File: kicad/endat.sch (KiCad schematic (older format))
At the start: 29 parts, among them J1901 tblock2x6, U1901 SI8662BD, U1904 SN75C1168DBR, U1905 SN75C1168DBR, U1908 SI8662BD

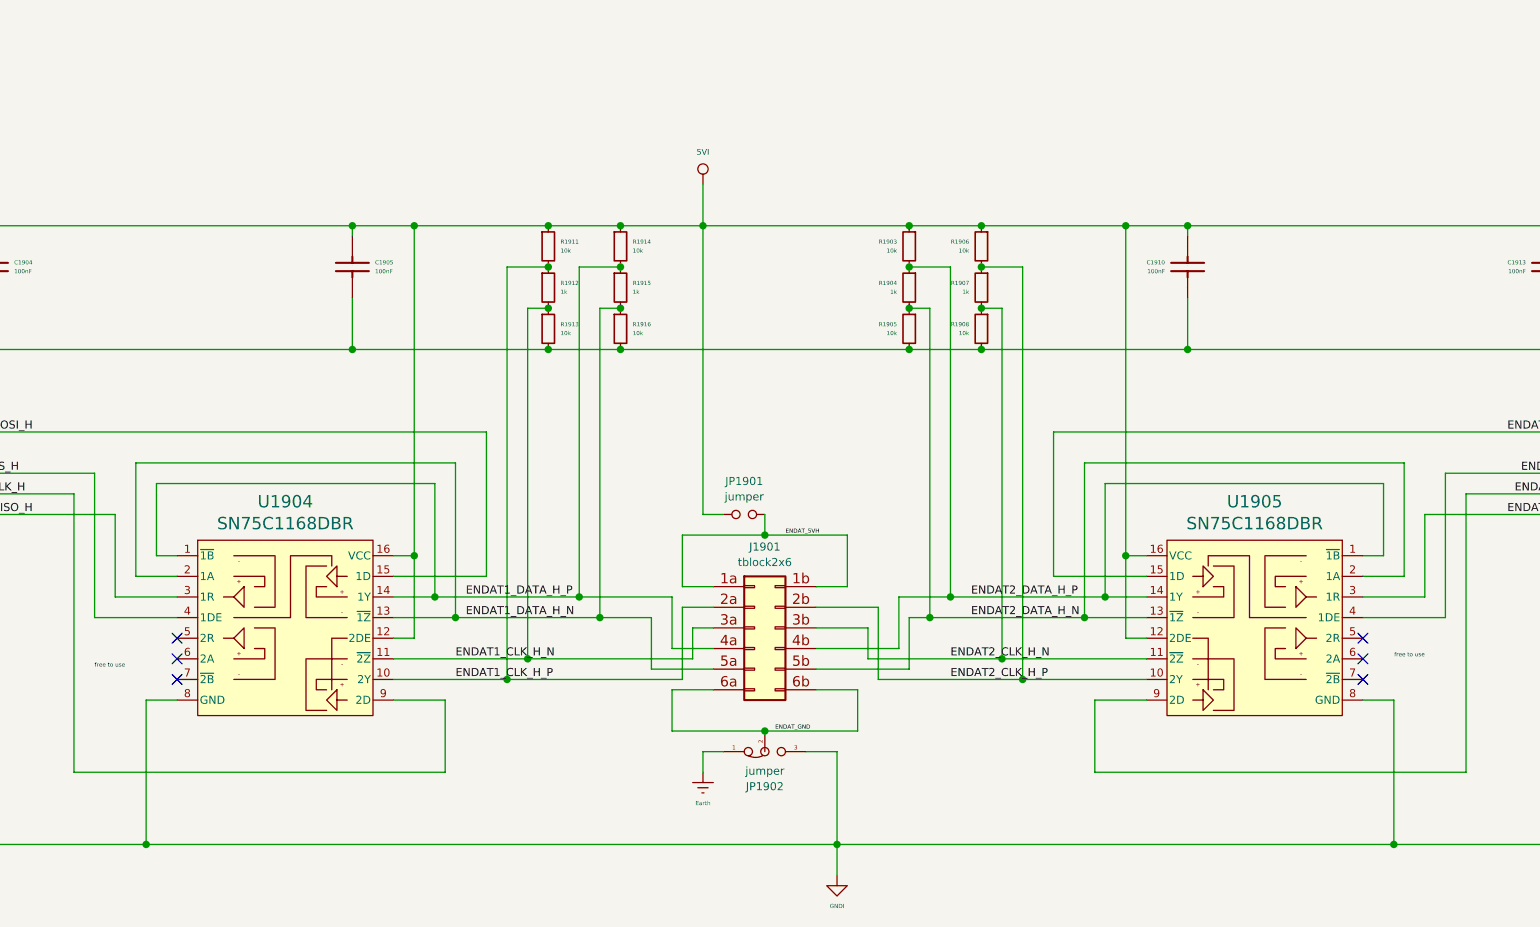
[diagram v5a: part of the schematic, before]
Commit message: added sloted holes everyware
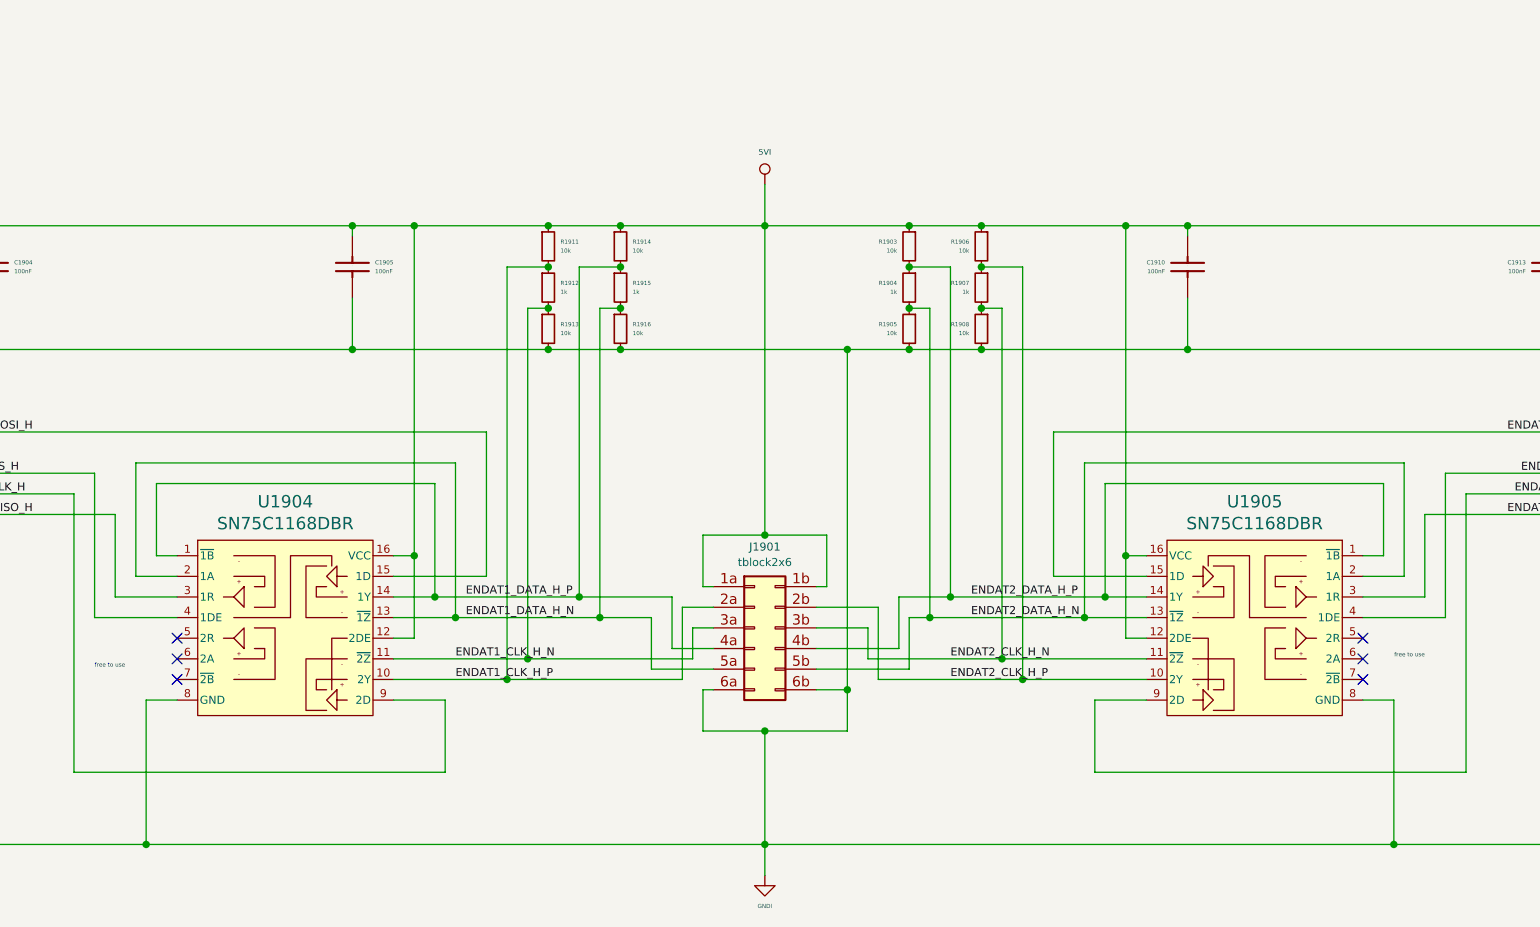
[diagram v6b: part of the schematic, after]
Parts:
- removed JP1901: jumper, servo:SolderJumper-2_P1.3mm_Open_RoundedPad1.0x1.5mm, symbol servo:jumper
- removed JP1902: jumper, Jumper:SolderJumper-3_P1.3mm_Open_RoundedPad1.0x1.5mm, symbol servo:Jumper_3_Bridged12
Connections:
- net ENDAT_5VH is gone; now on net 5VI: J1901.1a (Pin_1a), J1901.1b (Pin_1b)
- net ENDAT_GND is gone; now on net GNDI: J1901.6a (Pin_6a), J1901.6b (Pin_6b)
- net GNDI: now also C1904.1, C1905.1, C1910.1, C1913.1, R1905.2, R1908.2, R1913.2, R1916.2
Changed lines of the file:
@@
 free to use\n
 Wire Wire Line
-	8050 4550 8150 4550
-Wire Wire Line
-	7900 5400 8100 5400
+	8050 5400 8100 5400
 $Comp
 L servo:tblock2x6 J?
@@
 ENDAT1_CS_H
 Wire Wire Line
-	8100 4900 7950 4900
-Wire Wire Line
-	7950 4900 7950 4650
-Wire Wire Line
-	8750 4650 8750 4900
-Wire Wire Line
-	8750 4900 8600 4900
+	8100 4900 8050 4900
+Wire Wire Line
+	8050 4900 8050 4650
+Wire Wire Line
+	8650 4650 8650 4900
+Wire Wire Line
+	8650 4900 8600 4900
 Wire Wire Line
 	4300 4150 7000 4150
@@
 	9250 3350 9050 3350
 Connection ~ 9050 3350
-$Comp
-L servo:Jumper_3_Bridged12 JP?
-U 1 1 5E31EACF
-P 8350 5700
-AR Path="/5E1BAEAA/5E31EACF" Ref="JP?"  Part="1"
-AR Path="/5E21534F/5E31EACF" Ref="JP?"  Part="1"
-AR Path="/5DE3DF56/5E31EACF" Ref="JP?"  Part="1"
-AR Path="/5F8D42C2/5E31EACF" Ref="JP1902"  Part="1"
-F 0 "JP1902" H 8350 5869 39  0000 C CNN
-F 1 "jumper" H 8350 5794 39  0000 C CNN
-F 2 "Jumper:SolderJumper-3_P1.3mm_Open_RoundedPad1.0x1.5mm" H 8150 5500 50  0001 C CNN
-F 3 "~" H 8250 5600 50  0001 C CNN
-	1    8350 5700
-	1    0    0    1
-$EndComp
-Wire Wire Line
-	8550 5700 8700 5700
-$Comp
-L servo:Earth #PWR?
-U 1 1 5E31EAD8
-P 8050 5800
-AR Path="/5E21534F/5E31EAD8" Ref="#PWR?"  Part="1"
-AR Path="/5DE3DF56/5E31EAD8" Ref="#PWR?"  Part="1"
-AR Path="/5F8D42C2/5E31EAD8" Ref="#PWR0269"  Part="1"
-F 0 "#PWR0269" H 8050 5550 20  0001 C CNN
-F 1 "Earth" H 8050 5650 20  0000 C CNN
-F 2 "" H 8050 5800 50  0001 C CNN
-F 3 "~" H 8050 5800 50  0001 C CNN
-	1    8050 5800
-	1    0    0    -1
-$EndComp
-Wire Wire Line
-	7900 5600 8350 5600
-Wire Wire Line
-	7900 5400 7900 5600
-Wire Wire Line
-	8800 5400 8800 5600
-Connection ~ 8350 5600
-Wire Wire Line
-	8350 5600 8800 5600
+Wire Wire Line
+	8050 5400 8050 5600
+Wire Wire Line
+	8750 5400 8750 5600
 Text Label 6900 4950 0    39   ~ 0
 ENDAT1_DATA_H_P
@@
 ENDAT2_CLK_H_P
 Wire Wire Line
-	8600 5400 8800 5400
-$Comp
-L servo:jumper JP?
-U 1 1 5E2E6204
-P 8250 4550
-AR Path="/5DD76B18/5E2E6204" Ref="JP?"  Part="1"
-AR Path="/5F8D42C2/5E2E6204" Ref="JP1901"  Part="1"
-F 0 "JP1901" H 8250 4711 39  0000 C CNN
-F 1 "jumper" H 8250 4636 39  0000 C CNN
-F 2 "servo:SolderJumper-2_P1.3mm_Open_RoundedPad1.0x1.5mm" H 8150 4530 50  0001 C CNN
-F 3 "~" H 8250 4630 50  0001 C CNN
-	1    8250 4550
-	1    0    0    -1
-$EndComp
-Wire Wire Line
-	7950 4650 8350 4650
-Wire Wire Line
-	8350 4550 8350 4650
-Connection ~ 8350 4650
-Wire Wire Line
-	8350 4650 8750 4650
-Wire Wire Line
-	8050 5800 8050 5700
-Wire Wire Line
-	8050 5700 8150 5700
-Text Label 8450 4650 0    20   ~ 0
-ENDAT_5VH
-Text Label 8400 5600 0    20   ~ 0
-ENDAT_GND
+	8600 5400 8750 5400
 Text Label 4350 4150 0    39   ~ 0
 ENDAT1_MOSI_H
@@
 L servo:5VI #PWR?
 U 1 1 5E5DC4DB
-P 8050 2950
-F 0 "#PWR?" H 8050 2750 20  0001 C CNN
-F 1 "5VI" H 8050 3107 28  0000 C CNN
-F 2 "" H 8050 2950 50  0001 C CNN
-F 3 "" H 8050 2950 50  0001 C CNN
-	1    8050 2950
-	1    0    0    -1
-$EndComp
-Wire Wire Line
-	8050 2950 8050 3150
+P 8350 2950
+AR Path="/5DD76B18/5E5DC4DB" Ref="#PWR?"  Part="1"
+AR Path="/5F8D42C2/5E5DC4DB" Ref="#PWR0148"  Part="1"
+F 0 "#PWR0148" H 8350 2750 20  0001 C CNN
+F 1 "5VI" H 8350 3107 28  0000 C CNN
+F 2 "" H 8350 2950 50  0001 C CNN
+F 3 "" H 8350 2950 50  0001 C CNN
+	1    8350 2950
+	1    0    0    -1
+$EndComp
+Wire Wire Line
+	8350 2950 8350 3150
 Wire Wire Line
 	9400 3150 9050 3150
@@
 Connection ~ 9050 3150
 Wire Wire Line
-	9050 3150 8050 3150
-Connection ~ 8050 3150
-Wire Wire Line
-	8050 3150 8050 4550
-Wire Wire Line
-	8050 3150 7650 3150
+	9050 3150 8350 3150
 Wire Wire Line
 	7300 3150 6650 3150
@@
 Wire Wire Line
 	9400 3750 9050 3750
-Wire Wire Line
-	9050 3750 7650 3750
 Connection ~ 9050 3750
 Connection ~ 7650 3750
 $Comp
-L servo:GNDI #PWR?
+L servo:GNDI #PWR0149
 U 1 1 5E670415
-P 8700 6300
-F 0 "#PWR?" H 8700 6050 30  0001 C CNN
-F 1 "GNDI" H 8700 6151 20  0000 C CNN
-F 2 "" H 8700 6300 50  0001 C CNN
-F 3 "" H 8700 6300 50  0001 C CNN
-	1    8700 6300
-	1    0    0    -1
-$EndComp
-Wire Wire Line
-	8700 5700 8700 6150
-Wire Wire Line
-	11400 6150 8700 6150
+P 8350 6300
+F 0 "#PWR0149" H 8350 6050 30  0001 C CNN
+F 1 "GNDI" H 8350 6151 20  0000 C CNN
+F 2 "" H 8350 6300 50  0001 C CNN
+F 3 "" H 8350 6300 50  0001 C CNN
+	1    8350 6300
+	1    0    0    -1
+$EndComp
 Wire Wire Line
 	11400 5450 11400 6150
-Connection ~ 8700 6150
-Wire Wire Line
-	8700 6150 8700 6300
-Wire Wire Line
-	5350 6150 8700 6150
+Wire Wire Line
+	8350 6150 8350 6300
+Wire Wire Line
+	5350 6150 8350 6150
 Wire Wire Line
 	5350 5450 5350 6150
@@
 Connection ~ 4600 3150
 Connection ~ 6350 3150
+Wire Wire Line
+	8050 4650 8350 4650
+Connection ~ 8350 4650
+Wire Wire Line
+	8350 4650 8650 4650
+Wire Wire Line
+	8350 3150 8350 4650
+Connection ~ 8350 3150
+Wire Wire Line
+	7650 3150 8350 3150
+Wire Wire Line
+	8050 5600 8350 5600
+Connection ~ 8350 6150
+Wire Wire Line
+	8350 6150 11400 6150
+Wire Wire Line
+	8350 5600 8350 6150
+Connection ~ 8350 5600
+Wire Wire Line
+	8350 5600 8750 5600
+Wire Wire Line
+	8750 5400 8750 3750
+Wire Wire Line
+	7650 3750 8750 3750
+Connection ~ 8750 5400
+Connection ~ 8750 3750
+Wire Wire Line
+	8750 3750 9050 3750
 $EndSCHEMATC

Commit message: serigrafia...
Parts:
- R1901, R1902, R1903, R1904, R1905, R1906, R1907, R1908, R1911, R1912, R1913, R1914, R1915, R1916, R1931, R1932: footprint Resistor_SMD:R_0603_1608Metric -> servo:R_0603_1608Metric
- U1904, U1905: footprint Package_SO:SOIC-16W_5.3x10.2mm_P1.27mm -> servo:SOIC-16W_5.3x10.2mm_P1.27mm
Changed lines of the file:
@@
 F 0 "U1904" H 6025 5712 60  0000 C CNN
 F 1 "SN75C1168DBR" H 6025 5606 60  0000 C CNN
-F 2 "Package_SO:SOIC-16W_5.3x10.2mm_P1.27mm" H 5900 5665 60  0001 C CNN
+F 2 "servo:SOIC-16W_5.3x10.2mm_P1.27mm" H 5900 5665 60  0001 C CNN
 F 3 "../doc/datasheets/sn65c1168.pdf" H 5900 5825 60  0001 C CNN
 	1    6000 5100
@@
 F 0 "R1902" H 2900 5815 20  0000 C CNN
 F 1 "0e(dnp)" H 2900 5772 20  0000 C CNN
-F 2 "Resistor_SMD:R_0603_1608Metric" H 2400 5600 60  0001 C CNN
+F 2 "servo:R_0603_1608Metric" H 2400 5600 60  0001 C CNN
 F 3 "" H 2500 5700 60  0001 C CNN
 	1    2900 5700
@@
 F 0 "R1901" H 2500 5815 20  0000 C CNN
 F 1 "0e" H 2500 5772 20  0000 C CNN
-F 2 "Resistor_SMD:R_0603_1608Metric" H 2000 5600 60  0001 C CNN
+F 2 "servo:R_0603_1608Metric" H 2000 5600 60  0001 C CNN
 F 3 "" H 2100 5700 60  0001 C CNN
 	1    2500 5700
@@
 F 0 "U1905" H 10775 5712 60  0000 C CNN
 F 1 "SN75C1168DBR" H 10775 5606 60  0000 C CNN
-F 2 "Package_SO:SOIC-16W_5.3x10.2mm_P1.27mm" H 10650 5665 60  0001 C CNN
+F 2 "servo:SOIC-16W_5.3x10.2mm_P1.27mm" H 10650 5665 60  0001 C CNN
 F 3 "../doc/datasheets/sn65c1168.pdf" H 10650 5825 60  0001 C CNN
 	1    10750 5100
@@
 F 0 "R1931" H 13850 5815 20  0000 C CNN
 F 1 "0e(dnp)" H 13850 5772 20  0000 C CNN
-F 2 "Resistor_SMD:R_0603_1608Metric" H 13350 5600 60  0001 C CNN
+F 2 "servo:R_0603_1608Metric" H 13350 5600 60  0001 C CNN
 F 3 "" H 13450 5700 60  0001 C CNN
 	1    13850 5700
@@
 F 0 "R1932" H 14250 5815 20  0000 C CNN
 F 1 "0e" H 14250 5772 20  0000 C CNN
-F 2 "Resistor_SMD:R_0603_1608Metric" H 13750 5600 60  0001 C CNN
+F 2 "servo:R_0603_1608Metric" H 13750 5600 60  0001 C CNN
 F 3 "" H 13850 5700 60  0001 C CNN
 	1    14250 5700
@@
 F 0 "R1911" H 7359 3272 20  0000 L CNN
 F 1 "10k" H 7359 3229 20  0000 L CNN
-F 2 "Resistor_SMD:R_0603_1608Metric" H 7300 3250 50  0001 C CNN
+F 2 "servo:R_0603_1608Metric" H 7300 3250 50  0001 C CNN
 F 3 "~" H 7300 3250 50  0001 C CNN
 	1    7300 3250
@@
 F 0 "R1912" H 7359 3472 20  0000 L CNN
 F 1 "1k" H 7359 3429 20  0000 L CNN
-F 2 "Resistor_SMD:R_0603_1608Metric" H 7300 3450 50  0001 C CNN
+F 2 "servo:R_0603_1608Metric" H 7300 3450 50  0001 C CNN
 F 3 "~" H 7300 3450 50  0001 C CNN
 	1    7300 3450
@@
 F 0 "R1913" H 7359 3672 20  0000 L CNN
 F 1 "10k" H 7359 3629 20  0000 L CNN
-F 2 "Resistor_SMD:R_0603_1608Metric" H 7300 3650 50  0001 C CNN
+F 2 "servo:R_0603_1608Metric" H 7300 3650 50  0001 C CNN
 F 3 "~" H 7300 3650 50  0001 C CNN
 	1    7300 3650
@@
 F 0 "R1914" H 7709 3272 20  0000 L CNN
 F 1 "10k" H 7709 3229 20  0000 L CNN
-F 2 "Resistor_SMD:R_0603_1608Metric" H 7650 3250 50  0001 C CNN
+F 2 "servo:R_0603_1608Metric" H 7650 3250 50  0001 C CNN
 F 3 "~" H 7650 3250 50  0001 C CNN
 	1    7650 3250
@@
 F 0 "R1915" H 7709 3472 20  0000 L CNN
 F 1 "1k" H 7709 3429 20  0000 L CNN
-F 2 "Resistor_SMD:R_0603_1608Metric" H 7650 3450 50  0001 C CNN
+F 2 "servo:R_0603_1608Metric" H 7650 3450 50  0001 C CNN
 F 3 "~" H 7650 3450 50  0001 C CNN
 	1    7650 3450
@@
 F 0 "R1916" H 7709 3672 20  0000 L CNN
 F 1 "10k" H 7709 3629 20  0000 L CNN
-F 2 "Resistor_SMD:R_0603_1608Metric" H 7650 3650 50  0001 C CNN
+F 2 "servo:R_0603_1608Metric" H 7650 3650 50  0001 C CNN
 F 3 "~" H 7650 3650 50  0001 C CNN
 	1    7650 3650
@@
 F 0 "R1906" H 9459 3272 20  0000 L CNN
 F 1 "10k" H 9459 3229 20  0000 L CNN
-F 2 "Resistor_SMD:R_0603_1608Metric" H 9400 3250 50  0001 C CNN
+F 2 "servo:R_0603_1608Metric" H 9400 3250 50  0001 C CNN
 F 3 "~" H 9400 3250 50  0001 C CNN
 	1    9400 3250
@@
 F 0 "R1907" H 9459 3472 20  0000 L CNN
 F 1 "1k" H 9459 3429 20  0000 L CNN
-F 2 "Resistor_SMD:R_0603_1608Metric" H 9400 3450 50  0001 C CNN
+F 2 "servo:R_0603_1608Metric" H 9400 3450 50  0001 C CNN
 F 3 "~" H 9400 3450 50  0001 C CNN
 	1    9400 3450
@@
 F 0 "R1908" H 9459 3672 20  0000 L CNN
 F 1 "10k" H 9459 3629 20  0000 L CNN
-F 2 "Resistor_SMD:R_0603_1608Metric" H 9400 3650 50  0001 C CNN
+F 2 "servo:R_0603_1608Metric" H 9400 3650 50  0001 C CNN
 F 3 "~" H 9400 3650 50  0001 C CNN
 	1    9400 3650
@@
 F 0 "R1903" H 9109 3272 20  0000 L CNN
 F 1 "10k" H 9109 3229 20  0000 L CNN
-F 2 "Resistor_SMD:R_0603_1608Metric" H 9050 3250 50  0001 C CNN
+F 2 "servo:R_0603_1608Metric" H 9050 3250 50  0001 C CNN
 F 3 "~" H 9050 3250 50  0001 C CNN
 	1    9050 3250
@@
 F 0 "R1904" H 9109 3472 20  0000 L CNN
 F 1 "1k" H 9109 3429 20  0000 L CNN
-F 2 "Resistor_SMD:R_0603_1608Metric" H 9050 3450 50  0001 C CNN
+F 2 "servo:R_0603_1608Metric" H 9050 3450 50  0001 C CNN
 F 3 "~" H 9050 3450 50  0001 C CNN
 	1    9050 3450
@@
 F 0 "R1905" H 9109 3672 20  0000 L CNN
 F 1 "10k" H 9109 3629 20  0000 L CNN
-F 2 "Resistor_SMD:R_0603_1608Metric" H 9050 3650 50  0001 C CNN
+F 2 "servo:R_0603_1608Metric" H 9050 3650 50  0001 C CNN
 F 3 "~" H 9050 3650 50  0001 C CNN
 	1    9050 3650

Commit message: serigraphi, improve of nets. change of soic 8 footprint
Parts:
- U1901, U1908: footprint Package_SO:SOIC-16W_7.5x10.3mm_P1.27mm -> servo:SOIC-16W_7.5x10.3mm_P1.27mm
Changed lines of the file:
@@
 F 0 "U1901" H 3600 4939 60  0000 C CNN
 F 1 "SI8662BD" H 3600 4833 60  0000 C CNN
-F 2 "Package_SO:SOIC-16W_7.5x10.3mm_P1.27mm" H 3000 4650 60  0001 C CNN
+F 2 "servo:SOIC-16W_7.5x10.3mm_P1.27mm" H 3000 4650 60  0001 C CNN
 F 3 "../doc/datasheets/Si8660.pdf" H 3500 4950 60  0001 C CNN
 	1    3600 4350
@@
 F 0 "U1908" H 13150 4939 60  0000 C CNN
 F 1 "SI8662BD" H 13150 4833 60  0000 C CNN
-F 2 "Package_SO:SOIC-16W_7.5x10.3mm_P1.27mm" H 12550 4650 60  0001 C CNN
+F 2 "servo:SOIC-16W_7.5x10.3mm_P1.27mm" H 12550 4650 60  0001 C CNN
 F 3 "../doc/datasheets/Si8660.pdf" H 13050 4950 60  0001 C CNN
 	1    13150 4350
